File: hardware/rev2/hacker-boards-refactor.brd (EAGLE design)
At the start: 25.4 x 58.4 mm, 37 parts, among them J1 MICRO_USB_B_JST_MC5BR3-M404-4S

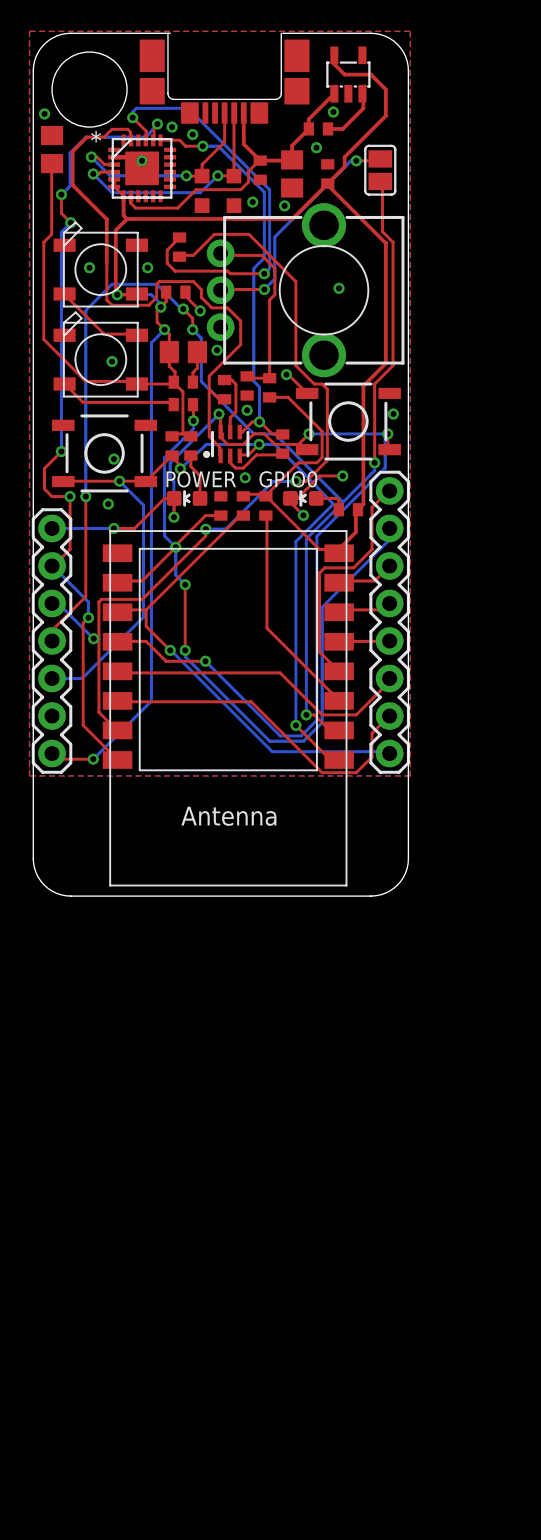
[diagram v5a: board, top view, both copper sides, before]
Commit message: Added huge solder stop area in the MHacks Refactor logo form
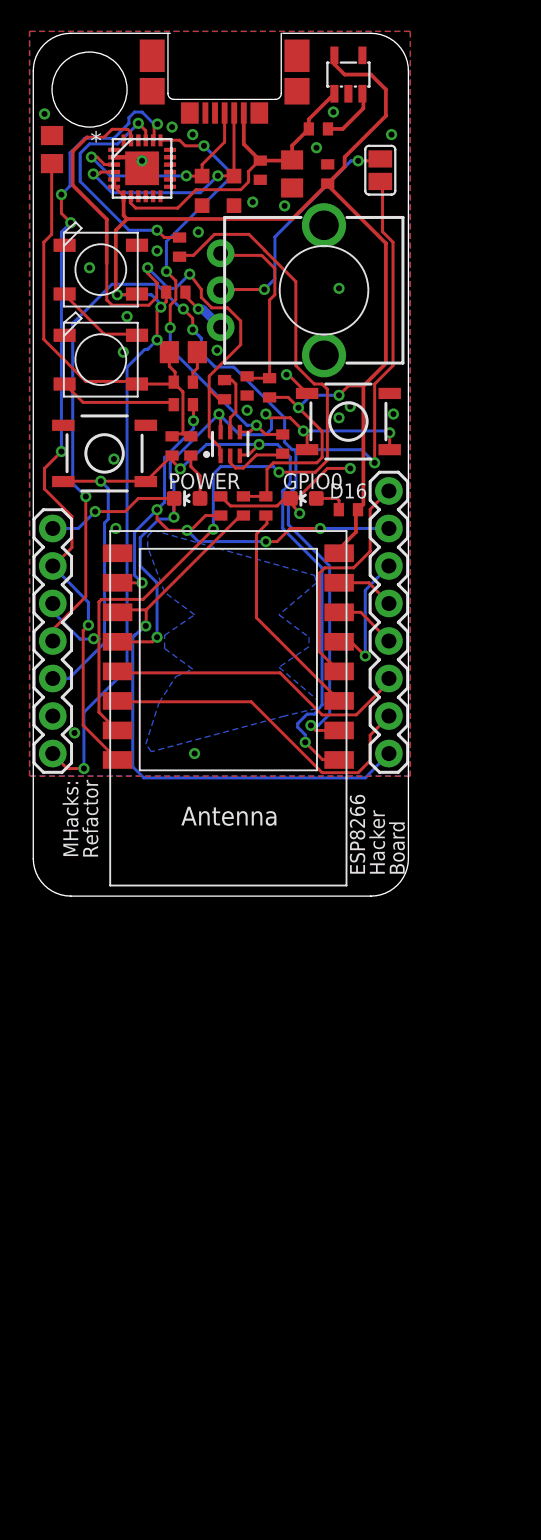
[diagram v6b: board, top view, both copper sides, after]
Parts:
- added U$5: (no value), hacker-board:EDGY-LOGO-8BIT
- moved JP3 0.05 mm to (1.32, 24.9)
- moved JP1 0.05 mm to (24.1, 27.4)
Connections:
- net GPIO12: now also JP1.5; no longer JP1.4
- net GPIO13: now also JP1.4; no longer JP1.3
- net GPIO14: now also JP1.3; no longer JP1.5
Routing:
- net GPIO0: track 73.8 -> 50.2 mm, vias 6 -> 7
- net GPIO15: track 54.7 -> 35.7 mm, vias 4 -> 6
- net USB_RX: track 28.8 -> 16.4 mm
- net GPIO2: track 32.5 -> 40.8 mm
- net GND: track 13.6 -> 21.1 mm, vias 22 -> 28
- net GPIO14: track 3.43 -> 8.93 mm, vias 0 -> 1
- net DTR: track 39.8 -> 43.0 mm, vias 0 -> 2
- net RTS: track 28.1 -> 31.1 mm, vias 2 -> 4
- net ANALOG_IN: track 91.4 -> 94.3 mm
- net RX: track 56.3 -> 58.9 mm
- net RST: track 61.6 -> 59.6 mm
- net +3V3: track 156.9 -> 156.1 mm, vias 4 -> 6
- net GPIO12: track 3.69 -> 4.38 mm
- net CH_PD: track 14.6 -> 15.2 mm
- net TX: track 54.5 -> 54.6 mm, vias 6 -> 5
- added copper zone on layer 16, net N$2
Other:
- board text added: "3V3"
- board text added: "A0"
- board text added: "D0"
- board text added: "D12"
- board text added: "D13"
- board text added: "D14"
- board text added: "D15"
- board text added: "D16"
- board text added: "D2"
- board text added: "D4"
- board text added: "D5"
- board text added: "ESP8266 Hacker Board"
- board text added: "GND"
- board text added: "Hacker Boards"
- board text added: "MHacks: Refactor"
- board text added: "RESET"
- board text added: "RX"
- board text added: "TX"
- board text added: "mhacks-hacker-boards.github.io"
- board text added: "rev 2.0"
